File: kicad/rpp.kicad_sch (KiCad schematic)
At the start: 13 parts, among them J1 SolderPad, J2 SolderPad, J3 SolderPad, J4 SolderPad, Q1 CSD19537Q3, U1 LM5050-1

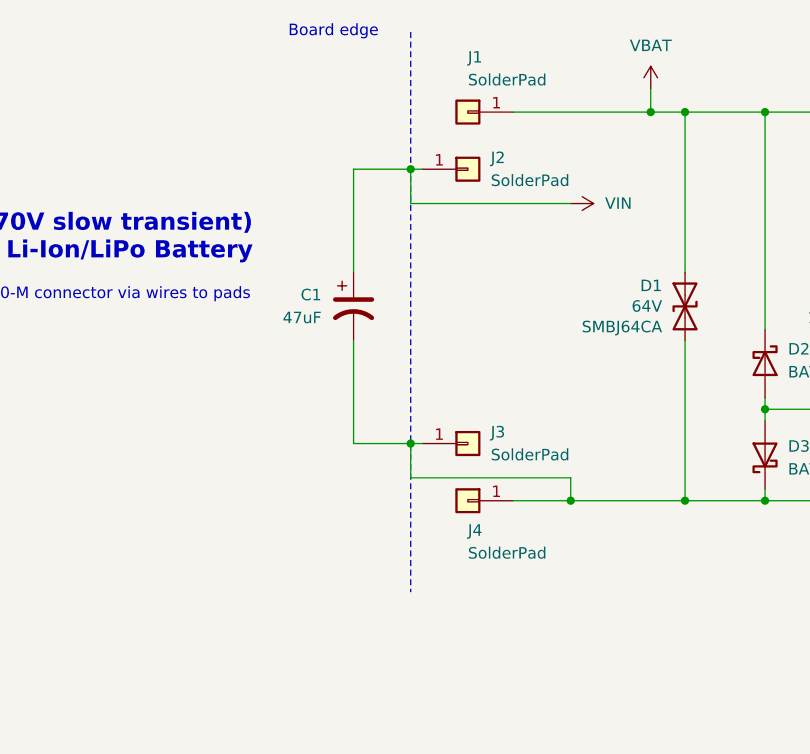
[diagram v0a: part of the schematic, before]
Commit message: Added heatsink footprint
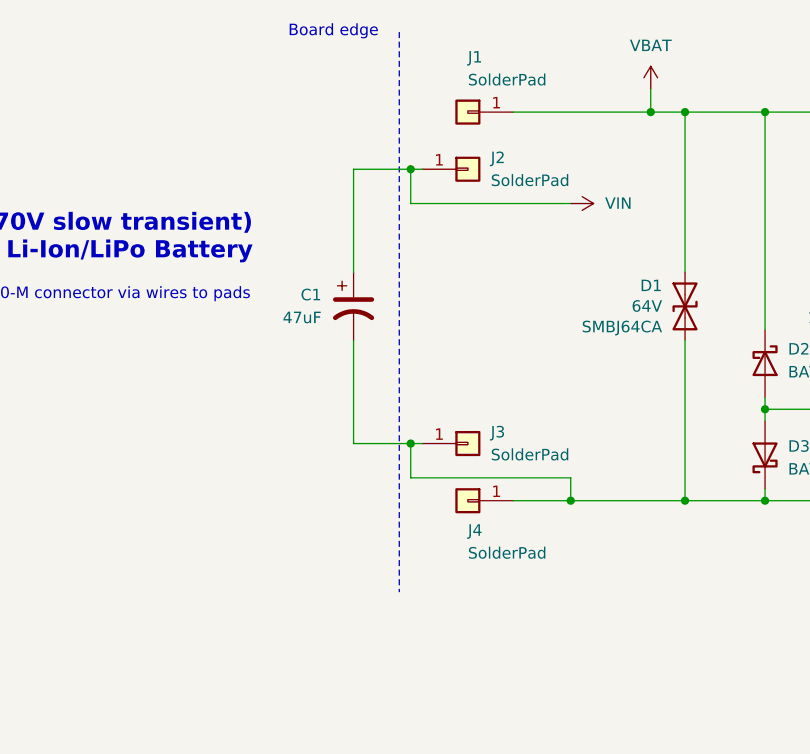
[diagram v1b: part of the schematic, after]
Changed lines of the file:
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@@
 	(polyline
 		(pts
-			(xy 116.84 69.85) (xy 116.84 132.08)
+			(xy 115.57 69.85) (xy 115.57 132.08)
 		)
 		(stroke
